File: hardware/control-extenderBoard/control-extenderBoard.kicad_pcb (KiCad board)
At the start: 2 copper layers, 100 x 100 mm, 72 parts, among them J1 SCL6 + GND (TP), J10 SCL6 + GND (TP), J11 SDA6 + GND (TP), J17 24V IN, J18 GND, J2 12V Out, J3 5V out, J4 SDA6 + GND (TP), J5 GND, J6 SCL7 Differential (TP), J7 SDA7 Differential (TP), J8 RS485, J9 3V3 out, P1 ISP, U1 MAX3485, U10 LM2576T-12, U2 PCA9600D, U3 TCA9548A_1-to-8_I2C_Multiplex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, U4 LM2576T-3.3, U5 PCA9600D, U6 PCA82C251, U7 PCA82C251, U8 PCA9600D, U9 LM2576T-5

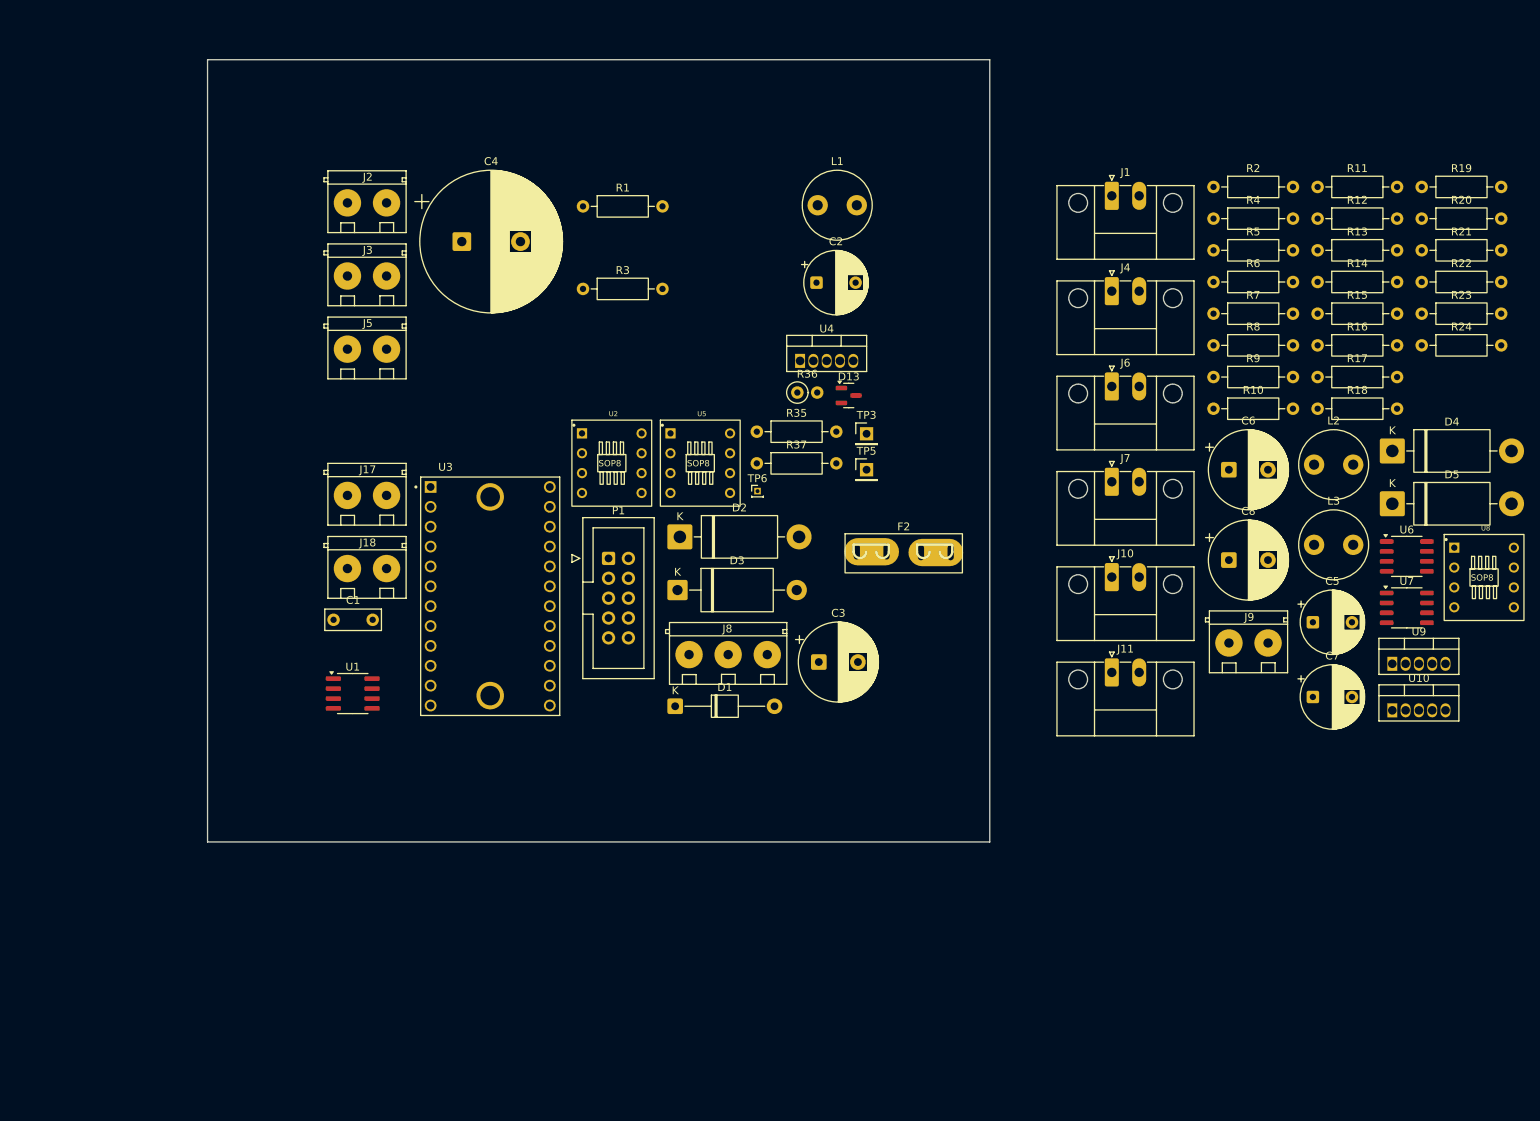
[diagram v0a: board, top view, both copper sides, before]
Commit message: extenderBoard: Add gyro board, Optimize i2c-boost + filter, Update footprints
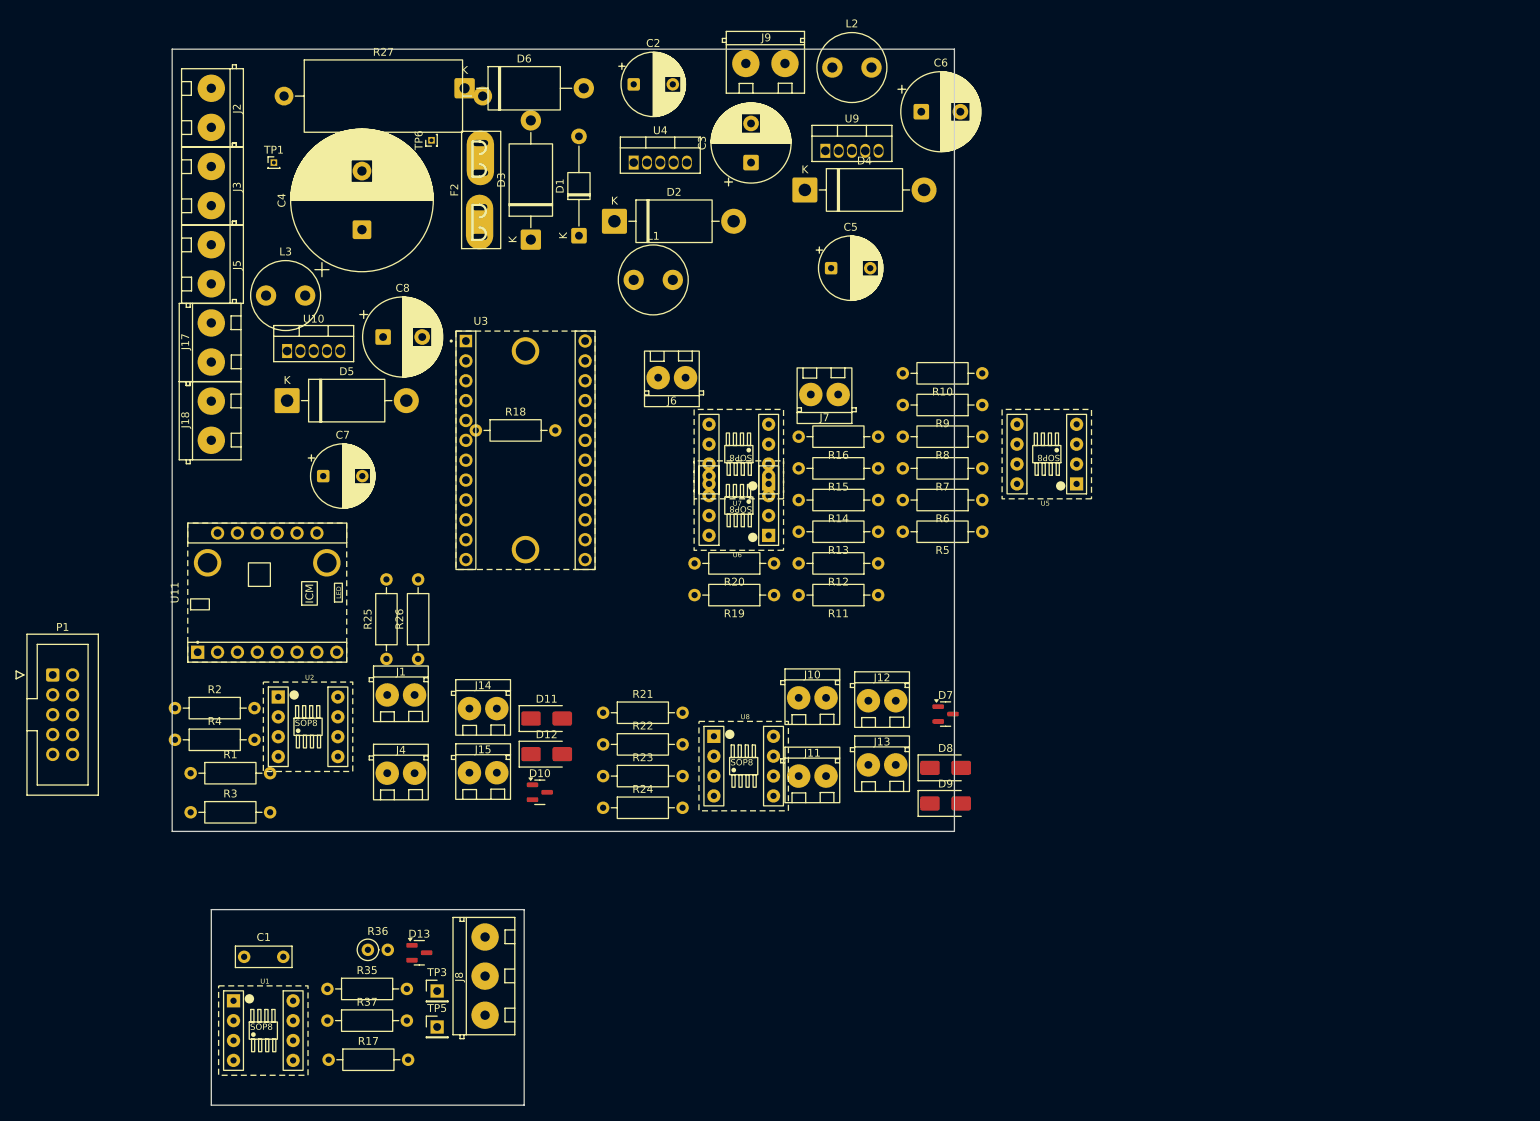
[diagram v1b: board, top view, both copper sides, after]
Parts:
- added D10: BAT54A, Package_TO_SOT_SMD:SOT-23, F.Cu at (92.0, 125.0)
- added D11: SMAJ150A, Diode_SMD:D_SMA, F.Cu at (92.9, 115.6)
- added D12: SMAJ150A, Diode_SMD:D_SMA, F.Cu at (92.9, 120.1)
- added D6: TVS 40V, Diode_THT:D_DO-201AE_P15.24mm_Horizontal, F.Cu at (82.4, 35.0)
- added D7: BAT54A, Package_TO_SOT_SMD:SOT-23, F.Cu at (143.9, 115.0)
- added D8: SMAJ150A, Diode_SMD:D_SMA, F.Cu at (143.9, 121.9)
- added D9: SMAJ150A, Diode_SMD:D_SMA, F.Cu at (143.9, 126.4)
- added J12: 3V3 + GND (TP), terminals_libJonny:ScrewTerminal_P3.5mm_2Pin_FP7x7, F.Cu at (134.0, 113.3)
- added J13: 12V + GND (TP), terminals_libJonny:ScrewTerminal_P3.5mm_2Pin_FP7x7, F.Cu at (134.0, 121.5)
- added J14: SCL6 + GND (TP), terminals_libJonny:ScrewTerminal_P3.5mm_2Pin_FP7x7, F.Cu at (83.0, 114.3)
- added J15: SDA6 + GND (TP), terminals_libJonny:ScrewTerminal_P3.5mm_2Pin_FP7x7, F.Cu at (83.0, 122.5)
- added R25: 2k2, Resistor_THT:R_Axial_DIN0207_L6.3mm_D2.5mm_P10.16mm_Horizontal, F.Cu at (72.4, 108.0)
- added R26: 2k2, Resistor_THT:R_Axial_DIN0207_L6.3mm_D2.5mm_P10.16mm_Horizontal, F.Cu at (76.4, 108.0)
- added R27: 2.5, Resistor_THT:R_Axial_DIN0922_L20.0mm_D9.0mm_P25.40mm_Horizontal, F.Cu at (59.3, 36.0)
- added TP1: 24V filtered, Connector_PinHeader_1.00mm:PinHeader_1x01_P1.00mm_Vertical, F.Cu at (58.0, 44.5)
- added U11: ICM-426XX_Breakout, modules_libJonny:ICM-426XX_6-Axis-Gyro_Breakout_Board, F.Cu at (57.1, 99.5)
- F2: value F-Servo -> F-total-control-supply
- J1: value SCL6 + GND (TP) -> 12V + GND (TP); footprint Connector_Phoenix_MC:PhoenixContact_MC_1,5_2-GF-3.5_1x02_P3.50mm_Horizontal_ThreadedFlange_MountHole -> terminals_libJonny:ScrewTerminal_P3.5mm_2Pin_FP7x7
- J10, J11, J6, J7: footprint Connector_Phoenix_MC:PhoenixContact_MC_1,5_2-GF-3.5_1x02_P3.50mm_Horizontal_ThreadedFlange_MountHole -> terminals_libJonny:ScrewTerminal_P3.5mm_2Pin_FP7x7
- J4: value SDA6 + GND (TP) -> 3V3 + GND (TP); footprint Connector_Phoenix_MC:PhoenixContact_MC_1,5_2-GF-3.5_1x02_P3.50mm_Horizontal_ThreadedFlange_MountHole -> terminals_libJonny:ScrewTerminal_P3.5mm_2Pin_FP7x7
- R1: value 1k -> 2k2
- R23, R24, R4: value 1k -> 750
- R3: value 2k2 -> 750
- U1: footprint Package_SO:SOIC-8_3.9x4.9mm_P1.27mm -> modules_libJonny:Adapter-Board_SOP8_to_DIP8
- U6, U7: footprint Package_SO:SO-8_3.9x4.9mm_P1.27mm -> modules_libJonny:Adapter-Board_SOP8_to_DIP8
- moved R17 153.6 mm to (65.0, 159.2)
- moved U10 148.6 mm to (59.7, 68.6)
- moved R2 148.5 mm to (45.4, 114.2)
- moved R4 148.5 mm to (45.4, 118.3)
- moved D5 141.9 mm to (59.7, 74.9)
- moved L3 137.7 mm to (57.0, 61.5)
- moved C7 129.6 mm to (64.3, 84.6)
- moved R23 120.2 mm to (100.1, 122.9)
- moved R24 120.2 mm to (100.1, 127.0)
- moved R21 120.2 mm to (100.1, 114.8)
- moved R22 120.2 mm to (100.1, 118.9)
- moved J1 112.5 mm to (72.5, 112.6)
- moved C8 111.8 mm to (72.0, 66.8)
- moved J4 111.3 mm to (72.5, 122.6)
- moved R18 107.6 mm to (83.8, 78.7)
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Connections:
- C1 pad 2: +24V filtered -> GNDPWR
- C2 pad 2: GND -> +24V filtered
- C3 pad 2: GND -> +24V filtered
- C5 pad 2: GND -> +24V filtered
- C6 pad 2: GND -> +24V filtered
- C7 pad 2: GND -> +24V filtered
- C8 pad 2: GND -> +24V filtered
- D1 pad 1: +24V filtered -> Net-(D1-K)
- D13 pad 3: GND -> +24V filtered
- D2 pad 2: GND -> +24V filtered
- D4 pad 2: GND -> +24V filtered
- D5 pad 2: GND -> +24V filtered
- F2 pad 1: +24V filtered -> Net-(D1-K)
- J1 pad 1: GND -> +12V
- J1 pad 2: Net-(J1-Pin_2) -> +24V filtered
- J10 pad 1: GND -> +24V filtered
- J11 pad 1: GND -> +24V filtered
- J18 pad 1: GND -> +24V filtered
- J18 pad 2: GND -> +24V filtered
- J4 pad 1: GND -> +3V3
- J4 pad 2: Net-(J4-Pin_2) -> +24V filtered
- J5 pad 1: GND -> +24V filtered
- J5 pad 2: GND -> +24V filtered
- J8 pad 1: GND -> +24V filtered
- R1 pad 1: +12V -> +3V3
- R1 pad 2: Net-(J4-Pin_2) -> /I2C5_SDA
- R12 pad 2: GND -> +24V filtered
- R2 pad 2: /I2C6_SCL -> /I2C5_SCL
- R3 pad 1: +3V3 -> +12V
- R3 pad 2: /I2C6_SDA -> Net-(D12-A1)
- R37 pad 2: GND -> +24V filtered
- R4 pad 2: Net-(J1-Pin_2) -> Net-(D11-A1)
- R5 pad 2: GND -> +24V filtered
- R6 pad 2: GND -> +24V filtered
- R9 pad 2: GND -> +24V filtered
- TP6 pad 1: +24V filtered -> Net-(D1-K)
- U1 pad 5: GND -> +24V filtered
- U10 pad 3: GND -> +24V filtered
- U10 pad 5: GND -> +24V filtered
- U2 pad 1: /I2C6_SCL -> /I2C5_SCL
- U2 pad 2: Net-(J1-Pin_2) -> Net-(D12-A1)
- U2 pad 3: Net-(J1-Pin_2) -> Net-(D12-A1)
- U2 pad 4: GND -> +24V filtered
- U2 pad 5: Net-(J4-Pin_2) -> Net-(D11-A1)
- U2 pad 6: Net-(J4-Pin_2) -> Net-(D11-A1)
- U2 pad 7: /I2C6_SDA -> /I2C5_SDA
- U3 pad 2: GND -> +24V filtered
- U3 pad 6: GND -> +24V filtered
- U3 pad 7: GND -> +24V filtered
- U3 pad 8: GND -> +24V filtered
- U4 pad 3: GND -> +24V filtered
- U4 pad 5: GND -> +24V filtered
- U5 pad 4: GND -> +24V filtered
- U6 pad 2: GND -> +24V filtered
- U7 pad 2: GND -> +24V filtered
- U8 pad 4: GND -> +24V filtered
- U9 pad 3: GND -> +24V filtered
- U9 pad 5: GND -> +24V filtered
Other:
- board size 100 x 100 mm -> 100 x 135 mm
